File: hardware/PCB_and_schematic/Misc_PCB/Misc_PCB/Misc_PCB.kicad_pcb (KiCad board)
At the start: 2 copper layers, 99.5 x 99.5 mm, 171 parts, among them J1 DIODE_BLINK_METER, J10 BATT, J11 ICP, J12 LCD_DISPLAY, J14 PROG_INTERFACE, J15 DS18B20, J16 DISPLAY, J18 LCD_CONN, J19 LCD16x2, J2 AC_IN, J3 DC_OUT, J4 LCD_CONN, J5 LCD_DISPLAY, J6 SOLAR_PANEL, J7 RS485, J8 THERMISTOR, J9 THERMISTOR, Q1 BC817, Q10 BC817, Q11 BC807, Q12 BC807, Q13 BC817, Q14 BC817, Q15 BC817, Q16 BT139-600, Q17 BC807, Q18 BC807, Q19 BC547, Q2 BC817, Q3 IRF540N, Q4 IRF540N, Q5 IRF540N, Q6 IRF540N, Q7 BC547, Q8 BC817, Q9 BC817, U1 LT4320xDD-1, U10 TL431LP, U11 ESP-07, U13 74HC595, U2 74HC595, U3 ST485, U4 INA226, U5 LT3652EMSE, U6 LM358, U7 INA226, U8 MC34063AP

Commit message: update power tracking heater
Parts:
- added C23: 470u/6,3V, Capacitor_SMD:CP_Elec_5x5.7, F.Cu at (171.2, 106.2)
- added C24: 100n, Capacitor_SMD:C_0805_2012Metric, B.Cu at (156.5, 124.2)
- added D10: D_Schottky, Diode_SMD:D_SMB, F.Cu at (19.8, 18.4)
- added D3: D_Schottky, Diode_SMD:D_SMB, F.Cu at (19.8, 7.33)
- added D6: D_Schottky, Diode_SMD:D_SMB, F.Cu at (19.8, 12.9)
- added F1: 1A, Fuse:Fuse_2010_5025Metric, B.Cu at (177.7, 101.8)
- added J13: PUSH_BUTTON, Connector_PinSocket_2.54mm:PinSocket_1x03_P2.54mm_Vertical, F.Cu at (176.6, 141.9)
- added J15: POWER_SUPPLY, Connector_PinSocket_2.54mm:PinSocket_1x02_P2.54mm_Vertical, F.Cu at (170.9, 99.0)
- added J17: 230V AC, TerminalBlock:TerminalBlock_bornier-4_P5.08mm, F.Cu at (217.7, 121.1)
- added L1: L, Inductor_SMD:L_Bourns_SRR1208_12.7x12.7mm, F.Cu at (31.8, 11.7)
- added R82: 10k, Resistor_SMD:R_0805_2012Metric_Pad1.20x1.40mm_HandSolder, B.Cu at (177.8, 137.8)
- added U12: AMS1117-3.3, Package_TO_SOT_SMD:SOT-223-3_TabPin2, B.Cu at (171.5, 107.6)
- added U13: MOC3033M, Package_DIP:DIP-6_W7.62mm_LongPads, F.Cu at (195.2, 130.3)
- added U9: PIC16F819-ISO, Package_SO:SOIC-18W_7.5x11.6mm_P1.27mm, F.Cu at (30.4, 25.5)
- D16: renamed from D14; moved to B.Cu
- D17: renamed from D15; moved to B.Cu
- D18: renamed from D16; moved to B.Cu
- D19: renamed from D17; moved to B.Cu
- Q13: renamed from Q17; moved to B.Cu
- Q14: renamed from Q18; moved to B.Cu
- Q15: renamed from Q13; footprint Package_TO_SOT_SMD:SOT-23_Handsoldering -> Package_TO_SOT_SMD:SOT-23; moved to B.Cu
- Q16: renamed from Q14; footprint Package_TO_SOT_SMD:SOT-23_Handsoldering -> Package_TO_SOT_SMD:SOT-23; moved to B.Cu
- Q17: renamed from Q15; footprint Package_TO_SOT_SMD:SOT-23_Handsoldering -> Package_TO_SOT_SMD:SOT-23; moved to B.Cu
- R48: renamed from R63; moved to B.Cu
- R49: renamed from R65; moved to B.Cu
- R50: renamed from R64; moved to B.Cu
- R51: renamed from R66; moved to B.Cu
- R52: renamed from R44; moved to B.Cu
- R53: renamed from R45; moved to B.Cu
- R54: renamed from R62; moved to B.Cu
- R55: renamed from R61; moved to B.Cu
- R56: renamed from R46; moved to B.Cu
- R57: renamed from R47; moved to B.Cu
- R58: renamed from R48; moved to B.Cu
- R59: renamed from R49; moved to B.Cu
- R60: renamed from R50; moved to B.Cu
- R61: renamed from R51; moved to B.Cu
- R63: renamed from R53; moved to B.Cu
- R64: renamed from R54; moved to B.Cu
- R69: renamed from R59; moved to B.Cu
- R70: renamed from R60; moved to B.Cu
- moved R52 261.3 mm to (148.4, 124.2), turned to 180 degrees
- moved J16 249.2 mm to (162.1, 141.3)
- moved J14 248.9 mm to (145.4, 141.3)
- moved D18 245.4 mm to (145.3, 103.2)
- moved Q15 242.0 mm to (146.8, 108.7), turned to 180 degrees
- moved R62 235.9 mm to (209.8, 142.4), turned to 90 degrees
- moved D16 235.4 mm to (159.1, 104.4)
- moved D17 233.8 mm to (161.3, 109.2), turned to -90 degrees
- moved R70 232.7 mm to (149.6, 103.6), turned to 90 degrees
- moved R55 232.5 mm to (166.0, 138.5), turned to 180 degrees
- moved R54 232.1 mm to (153.4, 116.8), turned to -90 degrees
- moved Q16 230.3 mm to (157.5, 108.7)
- moved D19 228.8 mm to (164.1, 109.2), turned to -90 degrees
- moved R69 228.5 mm to (143.5, 99.7), turned to 90 degrees
- moved R60 227.2 mm to (152.5, 107.5)
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- renumbered C9 to C10, C10 to C11, C11 to C12, C12 to C13, C13 to C14, C14 to C15, C15 to C16, C16 to C17, C17 to C18, C18 to C19, C19 to C20, C22 to C21, C20 to C22, C21 to C3, C3 to C4, C4 to C5, C5 to C6, C6 to C7, C7 to C8, C8 to C9, D18 to D14, D19 to D15, J16 to J14, J15 to J16, J14 to J18, J18 to J19, J19 to J20, Q16 to Q18, R6 to R10, R7 to R11, R8 to R12, R9 to R13, R10 to R14, R11 to R15, R12 to R16, R13 to R17, R14 to R18, R15 to R19, R16 to R20, R17 to R21, R18 to R22, R19 to R23, R20 to R24, R21 to R25, R22 to R26, R23 to R27, R24 to R28, R25 to R29, R26 to R30, R27 to R31, R28 to R32, R29 to R33, R30 to R34, R31 to R35, R32 to R36, R33 to R37, R34 to R38, R35 to R39, R36 to R40, R37 to R41, R38 to R42, R39 to R43, R40 to R44, R41 to R45, R42 to R46, R43 to R47, R71 to R5, R72 to R6, R52 to R62, R55 to R65, R56 to R66, R57 to R67, R58 to R68, R73 to R7, R67 to R71, R68 to R72, R69 to R73, R70 to R74, R74 to R8, R5 to R9, RV3 to RV2, RV2 to RV3, U13 to U14
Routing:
- net +3V3: track 0.00 -> 66.3 mm, vias 0 -> 7
- net RXD: track 0.00 -> 32.8 mm, vias 0 -> 2
- net Net-(D17-K): track 0.00 -> 27.9 mm, vias 0 -> 3
- net RST: track 0.00 -> 20.1 mm, vias 0 -> 1
- net MOSI: track 0.00 -> 15.7 mm
- net GPIO0: track 0.00 -> 15.5 mm, vias 0 -> 2
- net CS: track 0.00 -> 15.2 mm
- net CLK: track 0.00 -> 15.0 mm
- net TXD: track 0.00 -> 11.9 mm, vias 0 -> 1
- net Net-(D16-K): track 0.00 -> 8.70 mm
- net Net-(Q15-B): track 0.00 -> 4.01 mm
- net Net-(J18-Pin_1): track 0.00 -> 3.85 mm
- net Net-(U11-EN): track 0.00 -> 3.51 mm, vias 0 -> 1
- net Net-(U11-GPIO15): track 0.00 -> 3.34 mm, vias 0 -> 1
- net PUSH_BUTTON_1: track 0.00 -> 3.26 mm, vias 0 -> 1
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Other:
- board text added: "3V3"
- board text added: "ANTENNA KEEPOUT"
- board text added: "DTR"
- board text added: "ESP-07 ESP8266MOD"
- board text added: "PROGRAMMING INTERFACE"
- board text added: "RTS"
- board text added: "RX"
- board text added: "TX"

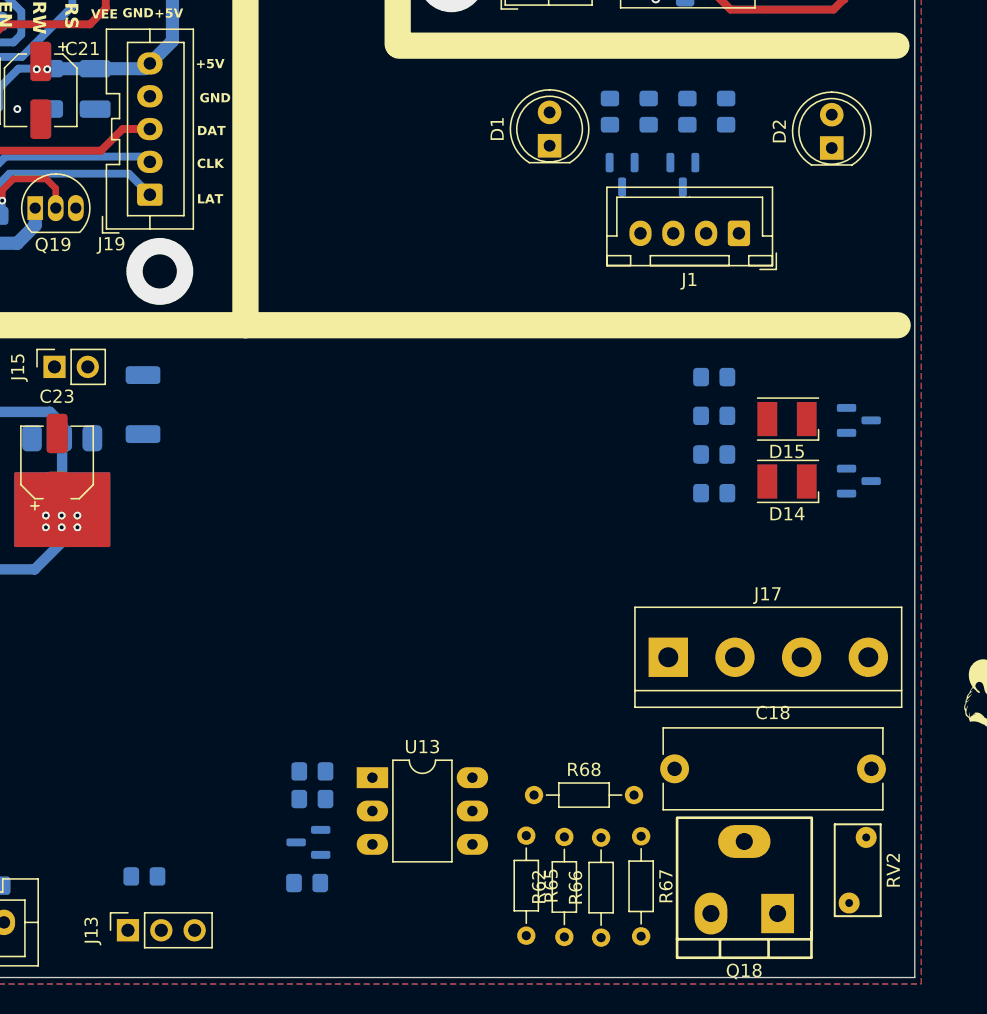
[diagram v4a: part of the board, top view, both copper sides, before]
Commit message: Parts chage for bms
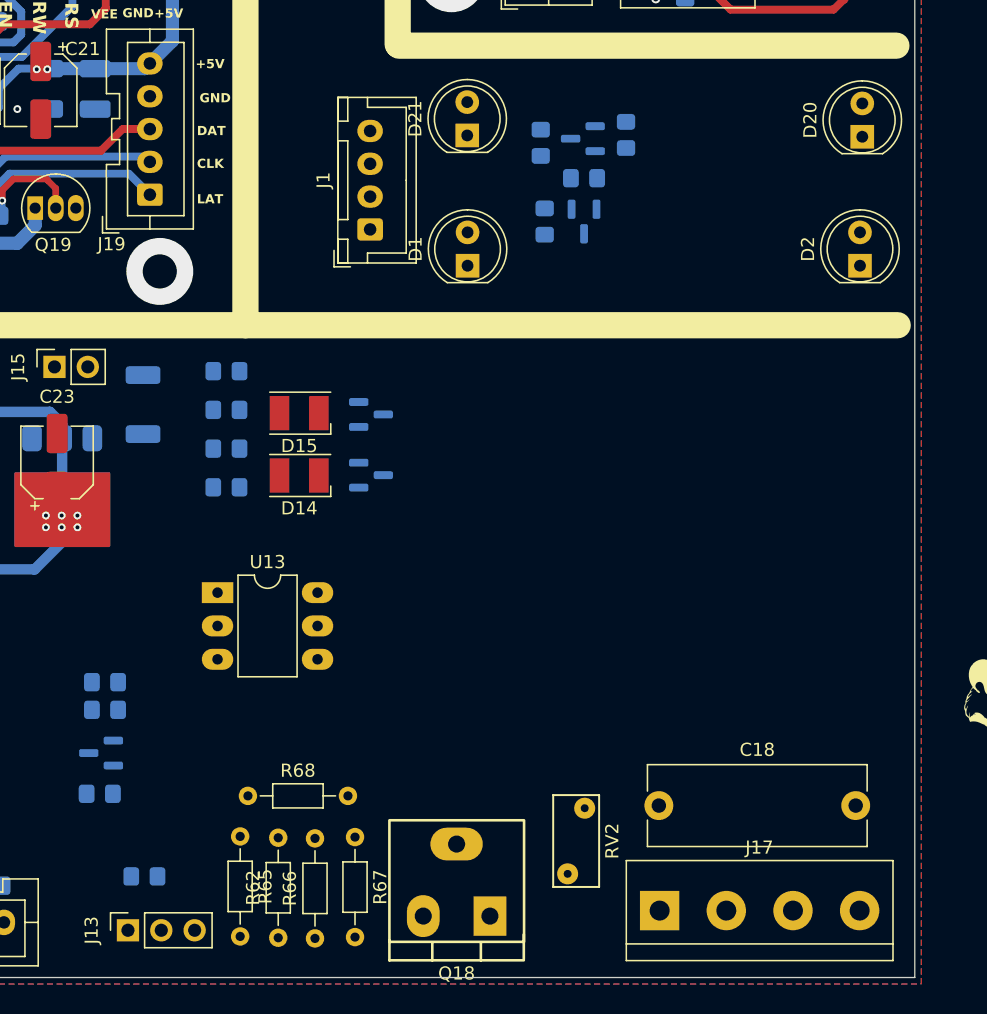
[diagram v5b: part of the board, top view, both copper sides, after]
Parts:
- added D20: BPV10, LED_THT:LED_D5.0mm, F.Cu at (232.5, 81.4)
- added D21: BPV10, LED_THT:LED_D5.0mm, F.Cu at (202.4, 81.3)
- moved D14 37.2 mm to (189.6, 107.2)
- moved D15 37.2 mm to (189.6, 102.5)
- moved Q13 37.2 mm to (195.1, 107.2)
- moved Q14 37.2 mm to (195.1, 102.6)
- moved R48 37.2 mm to (184.1, 108.2)
- moved R49 37.2 mm to (184.1, 102.2)
- moved R50 37.2 mm to (184.1, 105.2)
- moved R51 37.2 mm to (184.1, 99.3)
- moved J1 28.1 mm to (195.0, 88.5), turned to 90 degrees
- moved Q18 21.9 mm to (204.1, 140.9)
- moved R62 21.8 mm to (188.0, 142.5)
- moved R65 21.8 mm to (185.1, 134.8)
- moved R67 21.8 mm to (193.8, 134.8)
- moved R68 21.8 mm to (185.7, 131.7)
- moved R66 21.8 mm to (190.8, 142.5)
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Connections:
- net MISO renamed ZERO_CROSSING_SIGNAL

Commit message: power tracking heater progress
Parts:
- removed C18: 22n/250V AC, Capacitor_THT:C_Rect_L16.5mm_W6.0mm_P15.00mm_MKT
- removed C23: 470u/6,3V, Capacitor_SMD:CP_Elec_5x5.7
- removed C24: 100n, Capacitor_SMD:C_0805_2012Metric
- removed D14, D15: LED, LED_SMD:LED_PLCC-2_3.4x3.0mm_KA
- removed D16, D17, D18, D19: 3V3, Diode_SMD:D_MiniMELF
- removed F1: 1A, Fuse:Fuse_2010_5025Metric
- removed G***: LOGO, graphic:honeybadger2
- removed J13: PUSH_BUTTON, Connector_PinSocket_2.54mm:PinSocket_1x03_P2.54mm_Vertical
- removed J14: DISPLAY, Connector_JST:JST_XA_B05B-XASK-1_1x05_P2.50mm_Vertical
- removed J15: POWER_SUPPLY, Connector_PinSocket_2.54mm:PinSocket_1x02_P2.54mm_Vertical
- removed J16: DS18B20, Connector_JST:JST_XA_B03B-XASK-1_1x03_P2.50mm_Vertical
- removed J17: 230V AC, TerminalBlock:TerminalBlock_bornier-4_P5.08mm
- removed J18: PROG_INTERFACE, My-Footprints-connectors:Conn-01x06
- removed Q13, Q14: BC807, Package_TO_SOT_SMD:SOT-23
- removed Q15, Q16, Q17: BC817, Package_TO_SOT_SMD:SOT-23
- removed Q18: BT139-600, My-Footprints:TO-220-3_V_Wide_Legs
- removed R48, R49: 10K, Resistor_SMD:R_0805_2012Metric_Pad1.20x1.40mm_HandSolder
- removed R50, R51: 220R, Resistor_SMD:R_0805_2012Metric_Pad1.20x1.40mm_HandSolder
- removed R52: 10k, Capacitor_SMD:C_0805_2012Metric
- removed R53, R54, R55, R56, R57, R60, R61, R82: 10k, Resistor_SMD:R_0805_2012Metric_Pad1.20x1.40mm_HandSolder
- removed R58: 47k, Resistor_SMD:R_0805_2012Metric_Pad1.20x1.40mm_HandSolder
- removed R59: 47R, Resistor_SMD:R_0805_2012Metric_Pad1.20x1.40mm_HandSolder
- removed R62, R65, R66, R67: 200R, Resistor_THT:R_Axial_DIN0204_L3.6mm_D1.6mm_P7.62mm_Horizontal
- removed R63, R64: 560R, Resistor_SMD:R_0805_2012Metric_Pad1.20x1.40mm_HandSolder
- removed R68: 390R, Resistor_THT:R_Axial_DIN0204_L3.6mm_D1.6mm_P7.62mm_Horizontal
- removed R69, R70: 1k, Resistor_SMD:R_0805_2012Metric_Pad1.20x1.40mm_HandSolder
- removed RV2: S10K275, Varistor:RV_Disc_D7mm_W3.5mm_P5mm
- removed U11: ESP-07, RF_Module:ESP-07
- removed U12: AMS1117-3.3, Package_TO_SOT_SMD:SOT-223-3_TabPin2
- removed U13: MOC3033M, Package_DIP:DIP-6_W7.62mm_LongPads
- moved U5 125.6 mm to (175.1, 120.0)
- moved J11 78.7 mm to (63.9, 131.6)
- moved J7 78.7 mm to (73.4, 131.6)
- moved C11 78.7 mm to (103.7, 121.4)
- moved C12 78.7 mm to (59.1, 97.0)
- moved C13 78.7 mm to (126.5, 109.1)
- moved C15 78.7 mm to (68.6, 142.8)
- moved C17 78.7 mm to (122.4, 123.0)
- moved C6 78.7 mm to (81.4, 107.8)
- moved C8 78.7 mm to (68.6, 133.8)
- moved C9 78.7 mm to (68.6, 136.8)
- moved D10 78.7 mm to (77.8, 71.6)
- moved D11 78.7 mm to (93.2, 96.3)
- moved D12 78.7 mm to (100.7, 96.3)
- moved D13 78.7 mm to (108.2, 96.3)
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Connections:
- D20 pad 1: unconnected-(D20-K-Pad1) -> +5V
- D21 pad 1: unconnected-(D21-K-Pad1) -> +5V
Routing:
- net +3V3: track 66.3 -> 0.00 mm, vias 7 -> 0
- net RXD: track 32.8 -> 0.00 mm, vias 2 -> 0
- net Net-(D17-K): track 27.9 -> 0.00 mm, vias 3 -> 0
- net RST: track 20.1 -> 0.00 mm, vias 1 -> 0
- net MOSI: track 15.7 -> 0.00 mm
- net GPIO0: track 15.5 -> 0.00 mm, vias 2 -> 0
- net CS: track 15.2 -> 0.00 mm
- net CLK: track 15.0 -> 0.00 mm
- net TXD: track 11.9 -> 0.00 mm, vias 1 -> 0
- net +5V: track 107.8 -> 116.9 mm
- net Net-(D16-K): track 8.70 -> 0.00 mm
- net Net-(Q15-B): track 4.01 -> 0.00 mm
- net Net-(J18-Pin_1): track 3.85 -> 0.00 mm
- net Net-(U11-EN): track 3.51 -> 0.00 mm, vias 1 -> 0
- net Net-(U11-GPIO15): track 3.34 -> 0.00 mm, vias 1 -> 0
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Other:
- board text removed: "3V3"
- board text removed: "ANTENNA KEEPOUT"
- board text removed: "DTR"
- board text removed: "ESP-07 ESP8266MOD"
- board text removed: "PROGRAMMING INTERFACE"
- board text removed: "RTS"
- board text removed: "RX"
- board text removed: "TX"

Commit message: kicad oc
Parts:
- added J13: DIODE_BLINK_METER, Connector_JST:JST_XH_B4B-XH-A_1x04_P2.50mm_Vertical, B.Cu at (246.4, 76.7)
- added Q13: BC817, Package_TO_SOT_SMD:SOT-23, B.Cu at (240.5, 83.5)
- added Q14: BC817, Package_TO_SOT_SMD:SOT-23, B.Cu at (240.5, 88.1)
- added R48: 47k, Resistor_SMD:R_0805_2012Metric_Pad1.20x1.40mm_HandSolder, B.Cu at (245.3, 82.5)
- added R49: 47k, Resistor_SMD:R_0805_2012Metric_Pad1.20x1.40mm_HandSolder, B.Cu at (245.3, 85.5)
- added R50: 22k, Resistor_SMD:R_0805_2012Metric_Pad1.20x1.40mm_HandSolder, B.Cu at (245.3, 88.5)
- added R51: 22k, Resistor_SMD:R_0805_2012Metric_Pad1.20x1.40mm_HandSolder, B.Cu at (245.3, 91.4)
- J1: moved to B.Cu
- moved R4 3.83 mm to (206.4, 91.2), turned to 0 degrees
- moved R1 2.30 mm to (216.2, 79.7), turned to 0 degrees
- moved R3 1.60 mm to (206.5, 81.3), turned to 0 degrees
- moved Q1 1.24 mm to (211.9, 80.5)
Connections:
- D20 pad 2: unconnected-(D20-A-Pad2) -> Net-(D20-A)
- D21 pad 2: unconnected-(D21-A-Pad2) -> Net-(D21-A)

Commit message: LT3625 pcb
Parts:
- removed R16: 100m, Resistor_SMD:R_0805_2012Metric_Pad1.20x1.40mm_HandSolder
- added R53: 100m, Resistor_SMD:R_2512_6332Metric_Pad1.40x3.35mm_HandSolder, B.Cu at (188.9, 105.9)
- C10, C8, D3, D6, R21, R22, R23, R24, R26, R27, U5: moved to B.Cu
- C6: footprint Capacitor_THT:CP_Radial_D14.0mm_P5.00mm -> Capacitor_THT:CP_Radial_D10.0mm_P3.50mm
- R17, R30: value 100m -> 50m; footprint Resistor_SMD:R_0805_2012Metric_Pad1.20x1.40mm_HandSolder -> Resistor_SMD:R_2512_6332Metric_Pad1.40x3.35mm_HandSolder; moved to B.Cu
- R28: footprint Capacitor_SMD:C_1812_4532Metric -> Resistor_SMD:R_2512_6332Metric_Pad1.40x3.35mm_HandSolder; moved to B.Cu
- R38: footprint Capacitor_SMD:C_1825_4564Metric -> Resistor_SMD:R_4020_10251Metric_Pad1.65x5.30mm_HandSolder
- moved D7 217.7 mm to (310.5, 122.8)
- moved R26 217.7 mm to (281.1, 118.2), turned to 180 degrees
- moved R27 217.7 mm to (281.1, 121.2), turned to 180 degrees
- moved J10 217.7 mm to (296.3, 141.7)
- moved R30 125.4 mm to (193.4, 105.9), turned to -90 degrees
- moved R28 114.8 mm to (178.3, 103.2)
- moved C10 106.4 mm to (170.8, 110.1), turned to 90 degrees
- moved C8 102.7 mm to (166.0, 101.0), turned to 90 degrees
- moved D6 102.4 mm to (168.1, 114.3), turned to 180 degrees
- moved R24 99.6 mm to (163.4, 101.0), turned to -90 degrees
- moved R21 97.5 mm to (156.3, 107.9), turned to -90 degrees
- moved R23 96.7 mm to (160.4, 101.0), turned to -90 degrees
- moved R22 94.2 mm to (156.3, 112.0), turned to -90 degrees
- moved L1 93.5 mm to (172.5, 108.3), turned to 90 degrees
- moved U9 91.5 mm to (166.0, 127.2)
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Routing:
- net GND: track 43.6 -> 67.6 mm, vias 29 -> 35
- net Net-(D3-K): track 0.00 -> 18.5 mm
- net Net-(U5-V_{IN_REG}): track 0.00 -> 14.3 mm, vias 0 -> 2
- net CHRG: track 0.00 -> 7.72 mm
- net Net-(D6-K): track 0.00 -> 6.82 mm, vias 0 -> 8
- net SOLAR_CURRENT_LOW: track 0.00 -> 6.77 mm
- net FAULT: track 0.00 -> 6.06 mm
- net Net-(U5-TIMER): track 0.00 -> 4.72 mm
- net Net-(U5-SENSE): track 0.00 -> 3.96 mm, vias 0 -> 8
- net Net-(D7-K): track 0.00 -> 2.36 mm
